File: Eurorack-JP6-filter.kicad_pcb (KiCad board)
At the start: 2 copper layers, 65 x 100 mm, 138 parts, among them J1 JACK_MONO_SW, J2 JACK_MONO_SW, J3 JACK_MONO_SW, J4 JACK_MONO_SW, J5 JACK_MONO_SW, J6 JACK_MONO_SW, P1 CONN_02X05, Q1 BCM857BS, Q2 BCM857BS, Q3 J112, Q4 J112, Q5 J112, Q6 J112, SW1 KS-01Q, U1 TL072-, U10 CD4027, U11 CD40106, U2 TL072-, U3 TL072-, U4 TL072-, U5 LM13700, U6 LM13700, U7 LM13700, U8 DG409, U9 CD4052

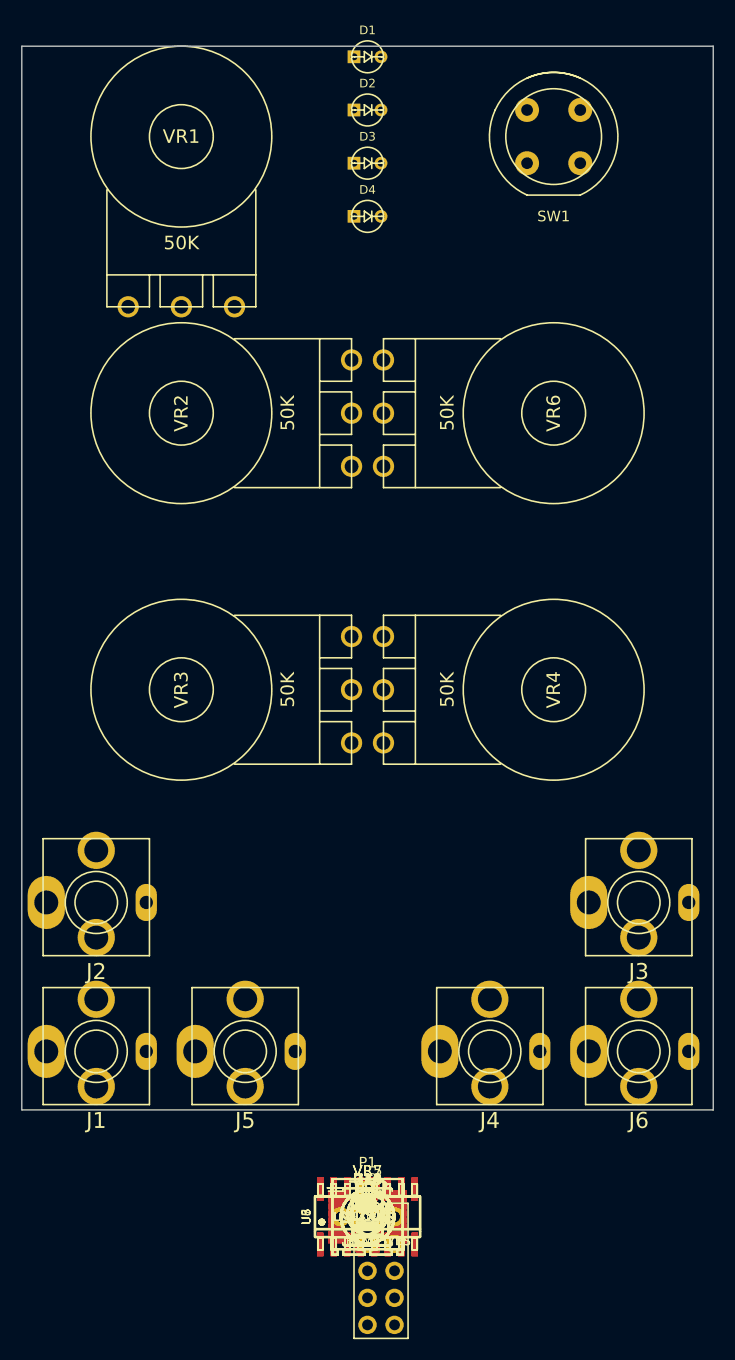
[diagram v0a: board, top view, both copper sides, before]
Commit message: placing components, a few footprints updated
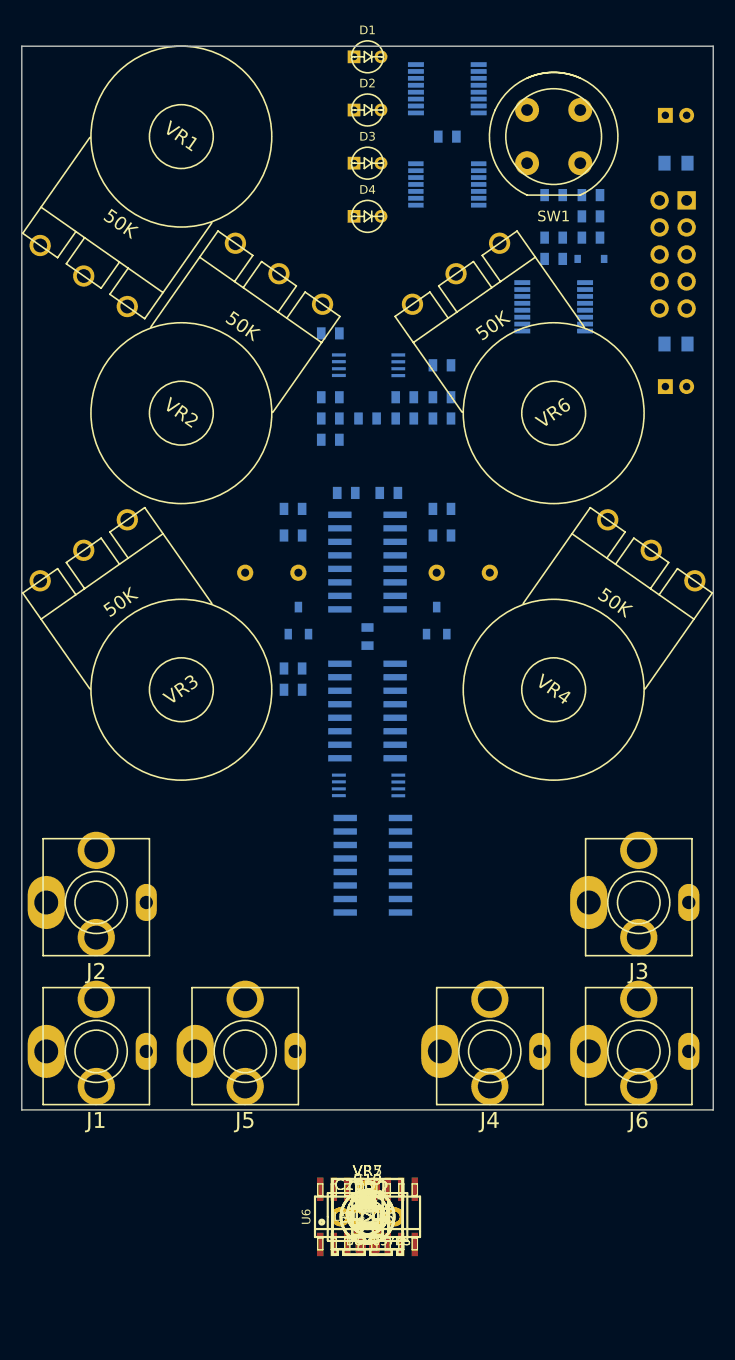
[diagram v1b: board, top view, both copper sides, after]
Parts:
- C1, C21, C22, C23, C24, C3, C4, D7, P1, Q3, Q4, R14, R18, R22, R24, R26, R29, R30, R32, R33, R37, R38, R39, R40, R41, R42, R58, R59, R61, R64, R7, R8, U10, U11, U3, U4, U5, U7, U8, U9: moved to B.Cu
- C18, C25: footprint MyModules:SM0603-C-JRL -> MyModules:CAP-BOX-PFR-5MM
- C6, C7: footprint MyModules:SM0603-C-JRL -> MyModules:CAP-BOX-PFR-5MM; moved to B.Cu
- R66, R67: footprint MyModules:SM0603-R-JRL -> MyModules:SM0805-HAND; moved to B.Cu
- moved C24 107.5 mm to (73.5, 18.5)
- moved U9 106.3 mm to (52.0, 16.0)
- moved R67 103.2 mm to (73.5, 23.0), turned to 180 degrees
- moved R41 101.8 mm to (52.0, 20.5), turned to 180 degrees
- moved P1 100.1 mm to (74.5, 26.5), turned to 180 degrees
- moved C21 98.3 mm to (65.5, 26.0)
- moved R64 97.6 mm to (62.0, 26.0), turned to 180 degrees
- moved U11 97.3 mm to (52.0, 25.0), turned to 180 degrees
- moved R58 96.4 mm to (65.5, 28.0)
- moved R61 94.4 mm to (65.5, 30.0)
- moved R59 93.7 mm to (62.0, 30.0)
- moved D7 92.5 mm to (65.5, 32.0), turned to 180 degrees
- moved C22 91.7 mm to (62.0, 32.0), turned to 180 degrees
- moved U10 87.3 mm to (62.0, 36.5), turned to 180 degrees
- moved R66 87.0 mm to (73.5, 40.0)
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
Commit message: components placed, beginning to route. current version crashes when 3D viewer is launched, going to try to open in previous version
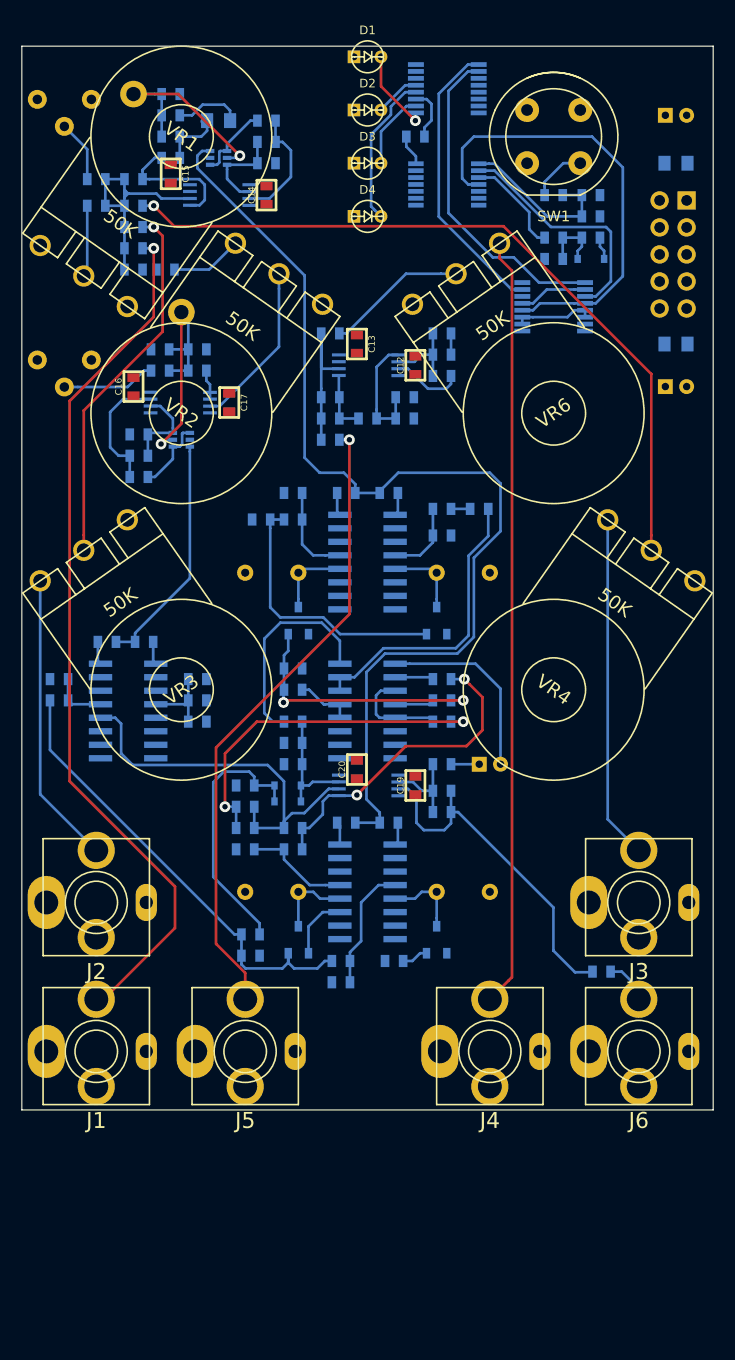
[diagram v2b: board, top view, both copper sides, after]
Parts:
- C10, C11, C18, C2, C25, C5, C8, C9, D5, D6, Q1, Q2, Q5, Q6, R1, R10, R11, R12, R13, R15, R16, R17, R2, R20, R21, R23, R25, R27, R28, R3, R31, R34, R35, R36, R4, R43, R44, R45, R46, R47, R48, R49, R5, R50, R51, R52, R53, R54, R55, R56, R57, R6, R60, R62, R63, R65, R68, R69, R70, R71, R72, R9, TP1, TP2, U1, U2, U6, VR5, VR7: moved to B.Cu
- R19: footprint MyModules:2MM-POL-CAP -> MyModules:SM0805-HAND; moved to B.Cu
- moved VR5 108.8 mm to (16.0, 17.0)
- moved TP2 107.8 mm to (22.5, 16.5)
- moved R25 107.2 mm to (26.0, 16.5), turned to 180 degrees
- moved R23 105.2 mm to (26.0, 18.5), turned to 180 degrees
- moved R19 104.0 mm to (30.5, 19.0), turned to 180 degrees
- moved R27 103.5 mm to (35.0, 19.0)
- moved R17 103.2 mm to (26.0, 20.5), turned to 180 degrees
- moved C5 101.5 mm to (35.0, 21.0), turned to 180 degrees
- moved R16 101.3 mm to (26.0, 22.5), turned to 180 degrees
- moved R6 100.8 mm to (19.0, 24.5), turned to 180 degrees
- moved Q2 100.5 mm to (30.5, 22.5), turned to 90 degrees
- moved R13 100.0 mm to (22.5, 24.5), turned to 180 degrees
- moved C15 99.8 mm to (26.0, 24.0), turned to 270 degrees
- moved R28 99.5 mm to (35.0, 23.0)
- moved R5 98.4 mm to (19.0, 27.0), turned to 180 degrees
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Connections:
- R47 pad 1: Net-(R47-Pad1) -> Net-(C11-Pad2)
- U4 pad 1: Net-(C11-Pad1) -> Net-(R48-Pad1)
- U4 pad 2: Net-(C11-Pad2) -> Net-(C8-Pad2)
- U4 pad 3: Net-(R47-Pad1) -> Net-(C9-Pad1)
- U4 pad 5: Net-(C9-Pad1) -> GND
- U4 pad 6: Net-(C8-Pad2) -> Net-(C11-Pad2)
- U4 pad 7: Net-(R48-Pad1) -> Net-(C11-Pad1)
- U7 pad 1: Net-(R56-Pad1) -> Net-(R68-Pad1)
- U7 pad 12: Net-(C25-Pad1) -> Net-(C18-Pad1)
- U7 pad 13: Net-(R63-Pad1) -> Net-(R52-Pad1)
- U7 pad 16: Net-(R68-Pad1) -> Net-(R56-Pad1)
- U7 pad 4: Net-(R52-Pad1) -> Net-(R63-Pad1)
- U7 pad 5: Net-(C18-Pad1) -> Net-(C25-Pad1)
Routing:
- net FREQ_CTRL: track 0.00 -> 99.6 mm
- net Net-(J1-Pad3): track 0.00 -> 82.5 mm, vias 0 -> 1
- net Net-(J4-Pad3): track 0.00 -> 72.4 mm
- net Net-(R4-Pad2): track 0.00 -> 71.0 mm, vias 0 -> 1
- net Net-(J5-Pad3): track 0.00 -> 59.9 mm, vias 0 -> 1
- net Net-(Q5-Pad1): track 0.00 -> 43.8 mm
- net Net-(U10-Pad12): track 0.00 -> 42.4 mm
- net Net-(C8-Pad2): track 0.00 -> 37.8 mm
- net Net-(C8-Pad1): track 0.00 -> 35.3 mm, vias 0 -> 2
- net Net-(R3-Pad2): track 0.00 -> 34.9 mm, vias 0 -> 1
- net Net-(C11-Pad1): track 0.00 -> 33.2 mm
- net Net-(J3-Pad3): track 0.00 -> 32.3 mm
- net Net-(U10-Pad1): track 0.00 -> 30.6 mm
- net Net-(R48-Pad1): track 0.00 -> 30.2 mm, vias 0 -> 2
- net SUM1: track 0.00 -> 27.7 mm
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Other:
- net class Default: clearance 0.2 -> 0.2032; trace_width 0.25 -> 0.254; via_dia 0.6 -> 1.016; via_drill 0.4 -> 0.508
- net class POWER added: clearance 0.254, trace_width 0.3556, via_dia 1.27, via_drill 0.635
- rule trace_clearance: 0.2 -> 0.2032

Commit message: routed most signals, still need to route power and ground
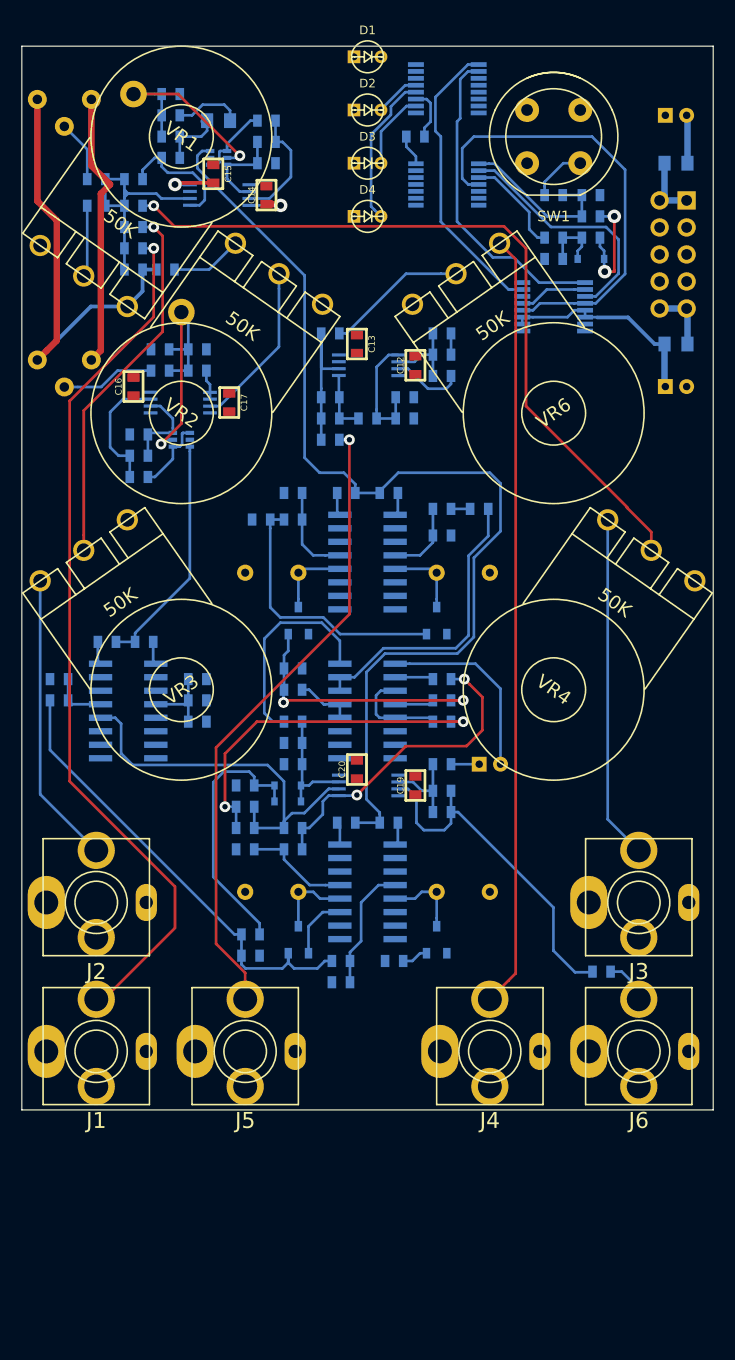
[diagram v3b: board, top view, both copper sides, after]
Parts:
- moved C15 4.00 mm to (30.0, 24.0)
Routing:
- net +12V: track 18.6 -> 86.2 mm, vias 0 -> 3
- net -12V: track 0.00 -> 35.6 mm, vias 0 -> 1
- net Net-(D1-Pad2): track 8.08 -> 0.00 mm, vias 1 -> 0
- net Net-(P1-Pad1): track 0.00 -> 6.23 mm
- net Net-(P1-Pad10): track 0.00 -> 5.91 mm
- net Net-(U10-Pad1): track 30.6 -> 30.0 mm
- net Net-(U10-Pad3): track 22.5 -> 23.1 mm

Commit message: routing power, swapped units on hex inverter
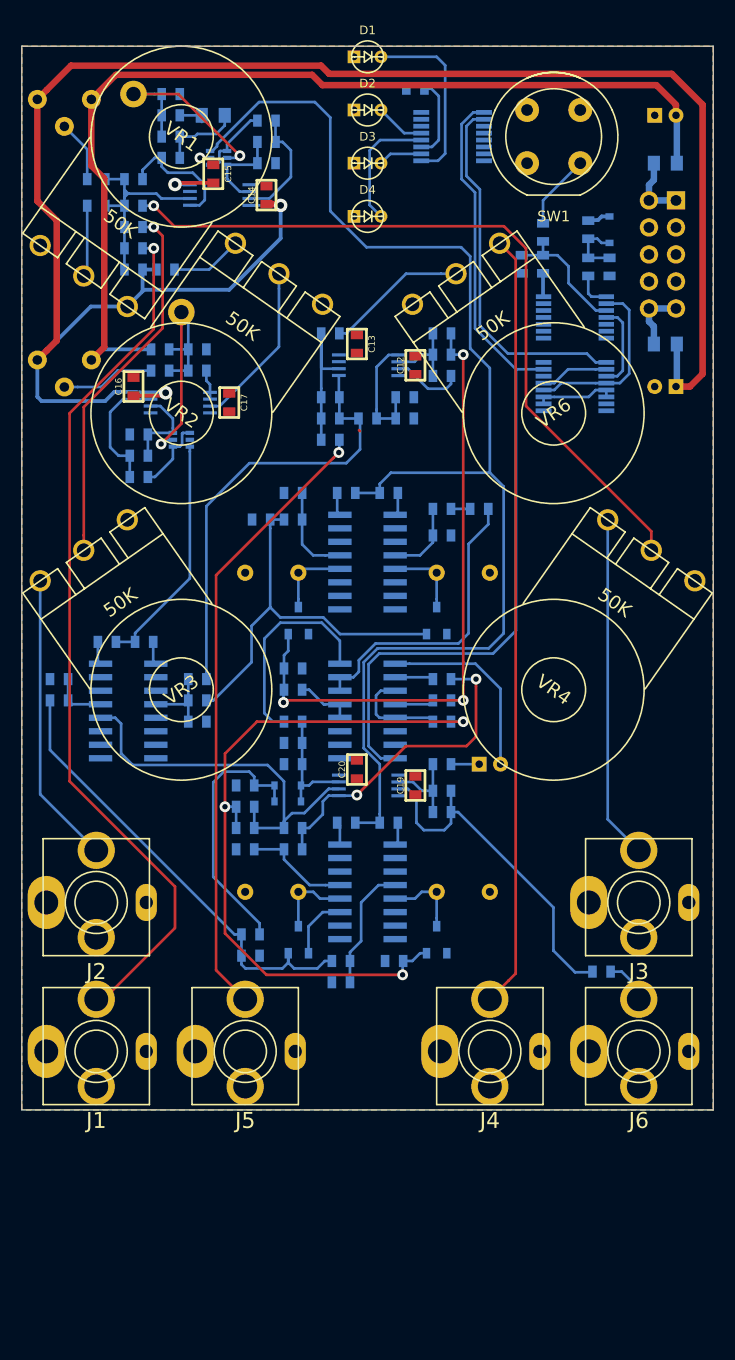
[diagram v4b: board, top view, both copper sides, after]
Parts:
- moved U11 17.3 mm to (64.0, 37.5)
- moved C21 9.19 mm to (59.0, 32.5), turned to 270 degrees
- moved U10 7.76 mm to (64.0, 44.0)
- moved R58 6.36 mm to (61.0, 32.5), turned to 270 degrees
- moved C22 5.30 mm to (67.2, 32.8), turned to 270 degrees
- moved U9 4.53 mm to (52.5, 20.5)
- moved R41 4.50 mm to (49.0, 16.0)
- moved R59 4.26 mm to (65.2, 32.8), turned to 90 degrees
- moved R64 3.64 mm to (61.0, 29.5), turned to 90 degrees
- moved D7 3.26 mm to (67.2, 29.2), turned to 270 degrees
- moved C23 1.00 mm to (72.5, 44.0), turned to 180 degrees
- moved C24 1.00 mm to (72.5, 18.5)
- moved P1 1.00 mm to (73.5, 26.5)
- moved R66 1.00 mm to (72.5, 40.0), turned to 180 degrees
- moved R67 1.00 mm to (72.5, 23.0)
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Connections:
- U11 pad 1: Net-(C21-Pad1) -> Net-(R59-Pad1)
- U11 pad 2: Net-(U10-Pad3) -> Net-(U10-Pad12)
- U11 pad 3: Net-(R59-Pad1) -> Net-(C21-Pad1)
- U11 pad 4: Net-(U10-Pad12) -> Net-(U10-Pad3)
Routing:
- net +12V: track 86.2 -> 199.3 mm, vias 3 -> 2
- net -12V: track 35.6 -> 99.2 mm
- net Net-(U10-Pad15): track 27.6 -> 80.7 mm
- net Net-(C1-Pad1): track 5.86 -> 41.7 mm
- net Net-(C3-Pad1): track 26.7 -> 60.4 mm, vias 2 -> 3
- net Net-(C8-Pad1): track 35.3 -> 66.9 mm, vias 2 -> 3
- net Net-(U10-Pad12): track 42.6 -> 17.1 mm
- net FREQ_CTRL: track 99.6 -> 120.8 mm
- net Net-(D1-Pad2): track 0.00 -> 17.2 mm
- net Net-(U10-Pad3): track 23.1 -> 8.02 mm
- net Net-(Q3-Pad1): track 25.3 -> 36.9 mm
- net Net-(R59-Pad1): track 9.48 -> 3.47 mm
- net Net-(U10-Pad1): track 30.0 -> 34.5 mm
- net Net-(R19-Pad1): track 6.32 -> 2.20 mm
- net Net-(C21-Pad1): track 15.5 -> 12.3 mm
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- added copper zone on B.Cu, net GND
- added copper zone on F.Cu, net GND

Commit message: still routing
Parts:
- moved TP1 6.10 mm to (32.0, 40.5)
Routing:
- net -12V: track 99.2 -> 241.5 mm, vias 1 -> 10
- net +12V: track 199.3 -> 292.9 mm, vias 2 -> 8
- net Net-(R4-Pad2): track 71.0 -> 74.6 mm
- net Net-(C8-Pad1): track 66.9 -> 64.4 mm
- net Net-(U2-Pad3): track 15.7 -> 17.9 mm
- net FREQ_CTRL: track 120.8 -> 122.9 mm
- net Net-(C5-Pad1): track 11.0 -> 12.9 mm
- net Net-(U10-Pad15): track 80.7 -> 79.8 mm
- net SWY2: track 18.0 -> 18.9 mm
- net OUT4: track 9.38 -> 8.59 mm
- net Net-(Q1-Pad5): track 23.8 -> 24.4 mm

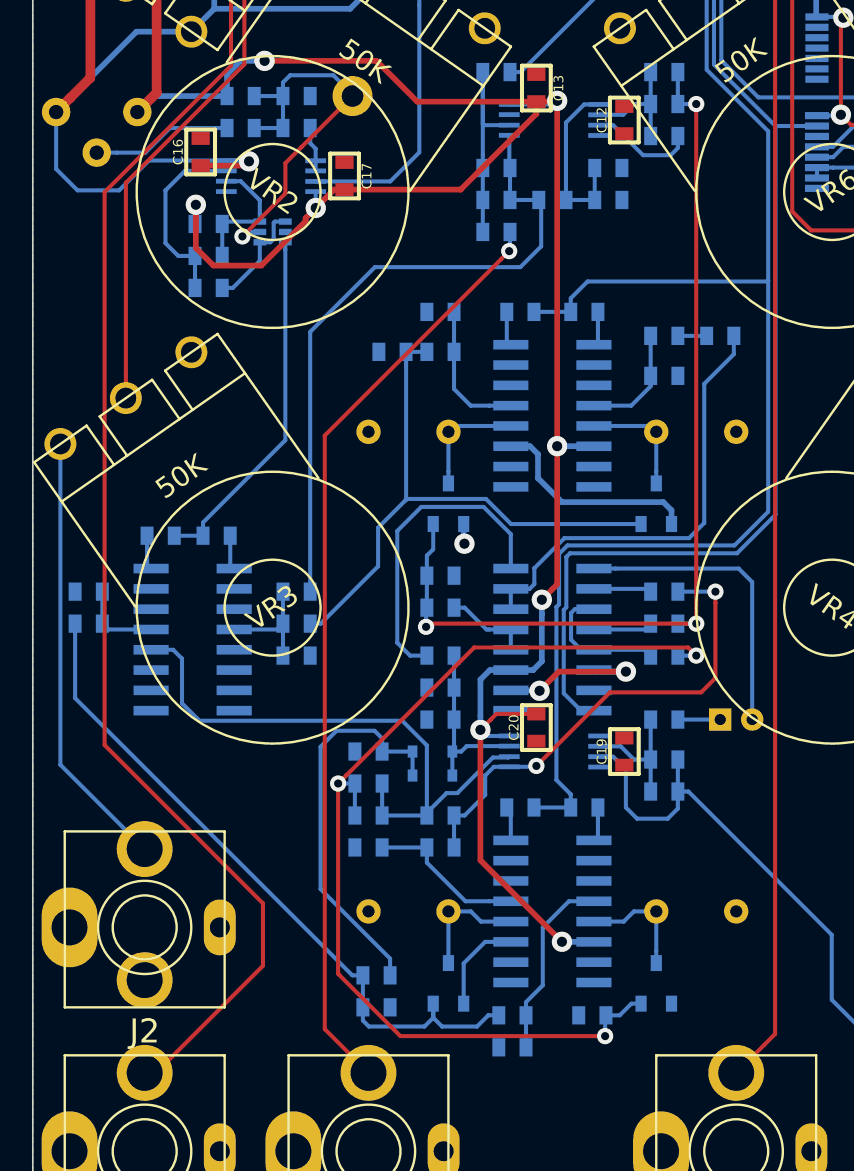
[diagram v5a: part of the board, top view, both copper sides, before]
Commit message: 8 connections left to route
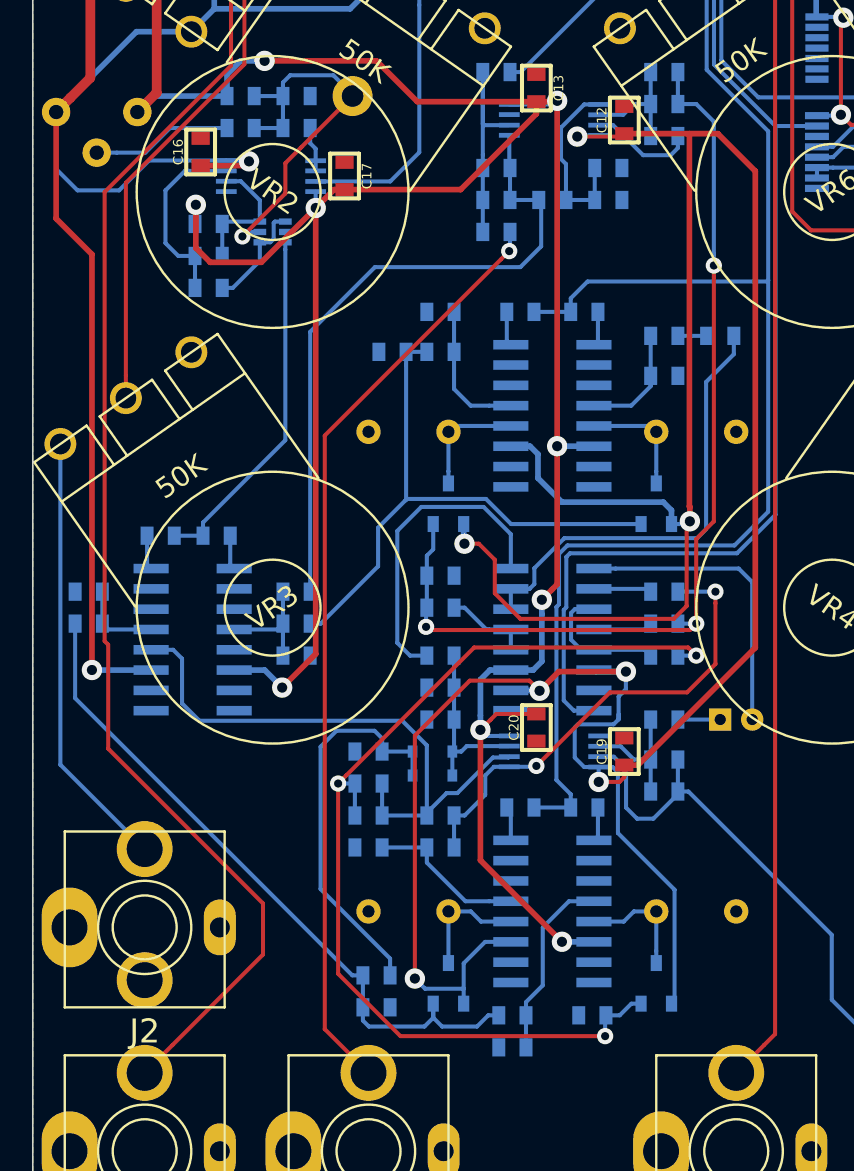
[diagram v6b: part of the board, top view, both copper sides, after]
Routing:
- net +12V: track 292.9 -> 494.1 mm, vias 8 -> 13
- net -12V: track 241.5 -> 275.5 mm, vias 10 -> 11
- net Net-(C3-Pad1): track 60.4 -> 61.5 mm
- net Net-(R48-Pad1): track 30.4 -> 29.9 mm
- net Net-(C11-Pad1): track 33.2 -> 32.7 mm

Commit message: routed, could still use refining
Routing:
- net Net-(C3-Pad2): track 7.53 -> 83.3 mm
- net Net-(U10-Pad1): track 34.5 -> 92.4 mm, vias 0 -> 4
- net +12V: track 494.1 -> 522.6 mm, vias 13 -> 14
- net GND: track 1.39 -> 15.9 mm, vias 1 -> 10
- net OUT4: track 8.59 -> 22.6 mm
- net Net-(R26-Pad1): track 8.47 -> 20.2 mm, vias 0 -> 2
- net -12V: track 275.5 -> 284.9 mm
- net Net-(C3-Pad1): track 61.5 -> 63.7 mm
- net FREQ_CTRL: track 122.9 -> 125.1 mm
- net Net-(C1-Pad1): track 41.7 -> 40.9 mm
- net SUM1: track 28.4 -> 29.1 mm
- net SWY2: track 18.9 -> 19.4 mm
- net Net-(J4-Pad3): track 72.7 -> 73.3 mm
- net Net-(C8-Pad2): track 37.5 -> 37.0 mm
- net Net-(Q3-Pad1): track 36.6 -> 37.1 mm
